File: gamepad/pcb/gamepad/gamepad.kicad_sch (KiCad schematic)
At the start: 13 parts, among them U3 RP2040-ZERO

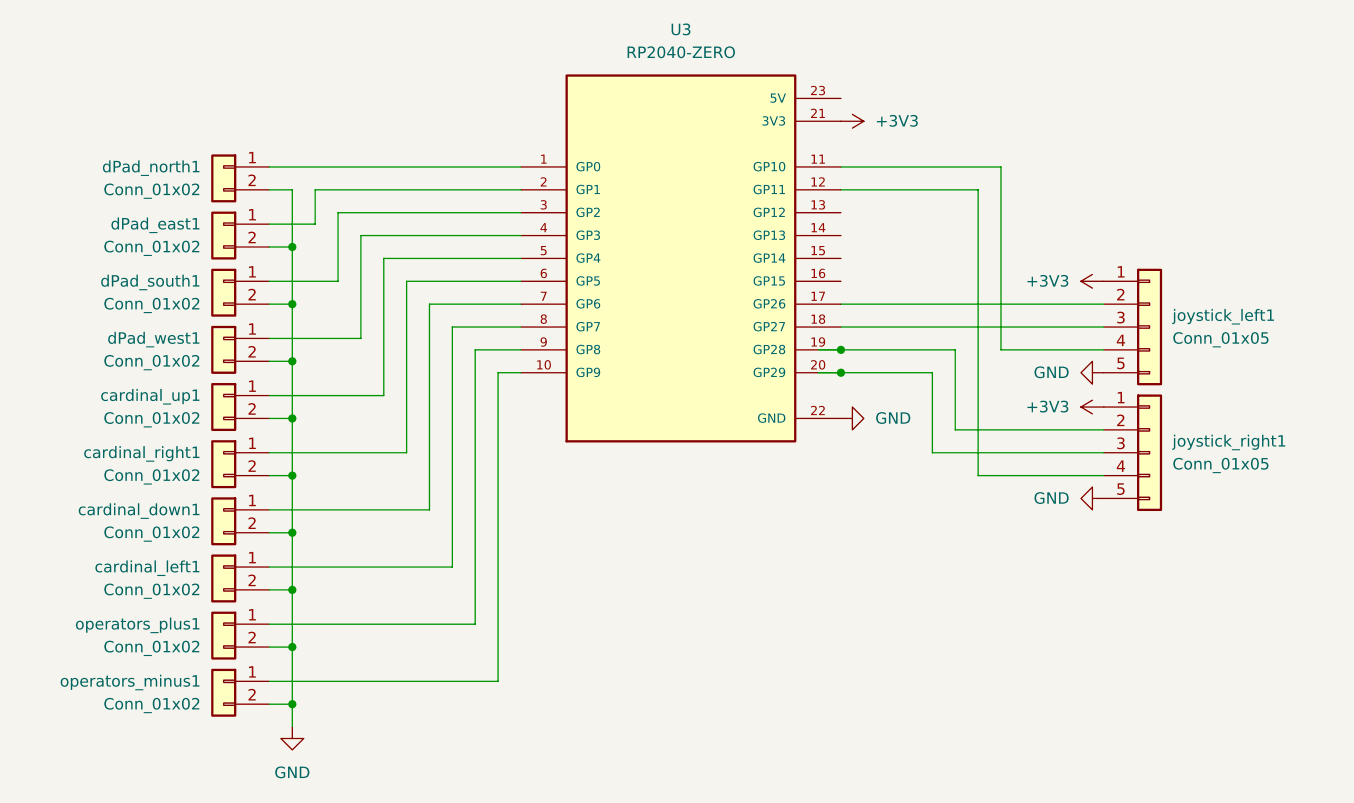
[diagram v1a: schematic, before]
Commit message: feat: smaller pcb
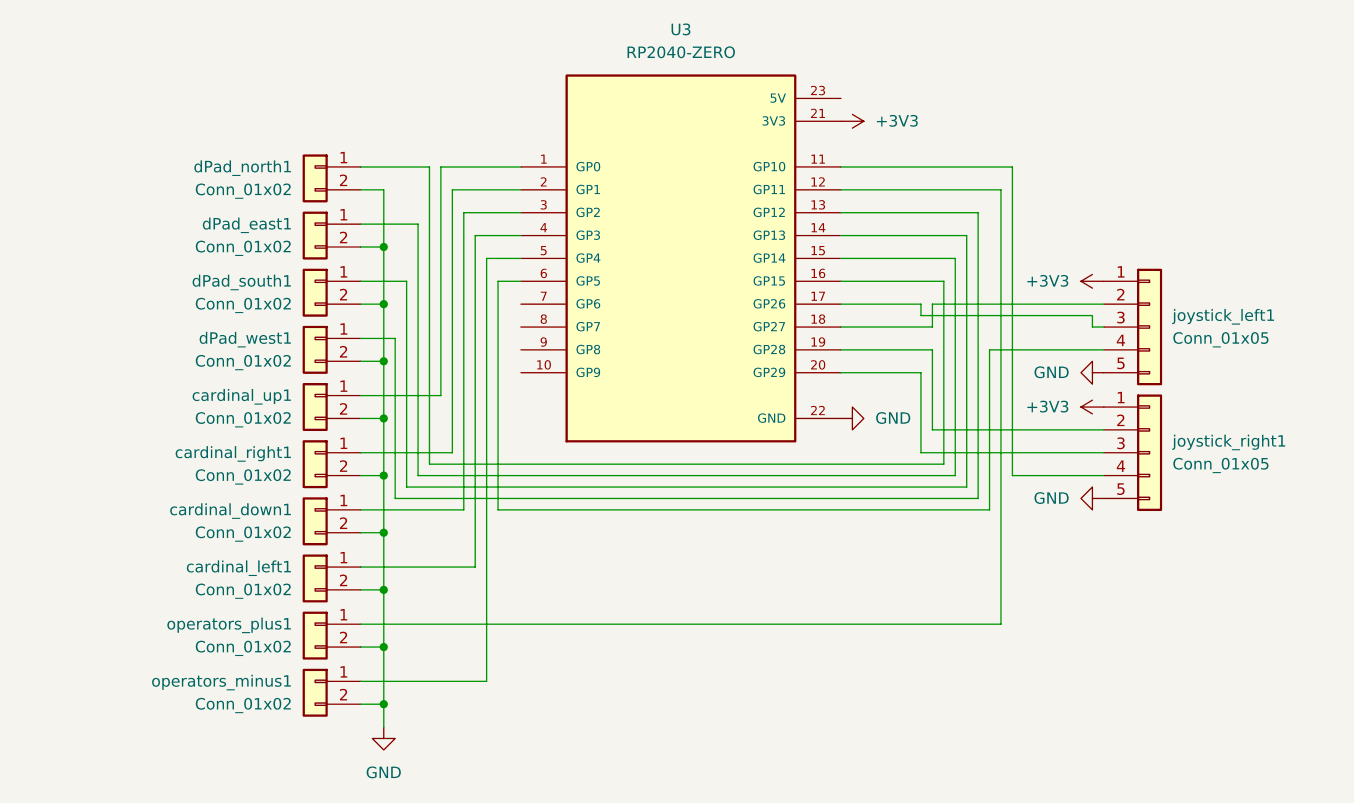
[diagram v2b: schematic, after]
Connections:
- net at operators_plus1.1 (Pin_1): now also U3.12 (GP11); no longer U3.9 (GP8)
- net at U3.1 (GP0): now also cardinal_up1.1 (Pin_1); no longer dPad_north1.1 (Pin_1)
- net at U3.10 (GP9): no longer operators_minus1.1 (Pin_1)
- net at U3.11 (GP10): now also joystick_right1.4 (Pin_4); no longer joystick_left1.4 (Pin_4)
- net at U3.13 (GP12): now also dPad_west1.1 (Pin_1)
- net at U3.14 (GP13): now also dPad_south1.1 (Pin_1)
- net at U3.15 (GP14): now also dPad_east1.1 (Pin_1)
- net at U3.16 (GP15): now also dPad_north1.1 (Pin_1)
- net at U3.17 (GP26): now also joystick_left1.3 (Pin_3); no longer joystick_left1.2 (Pin_2)
- net at U3.18 (GP27): now also joystick_left1.2 (Pin_2); no longer joystick_left1.3 (Pin_3)
- net at U3.2 (GP1): now also cardinal_right1.1 (Pin_1); no longer dPad_east1.1 (Pin_1)
- net at U3.3 (GP2): now also cardinal_down1.1 (Pin_1); no longer dPad_south1.1 (Pin_1)
- net at U3.4 (GP3): now also cardinal_left1.1 (Pin_1); no longer dPad_west1.1 (Pin_1)
- net at U3.5 (GP4): now also operators_minus1.1 (Pin_1); no longer cardinal_up1.1 (Pin_1)
- net at U3.6 (GP5): now also joystick_left1.4 (Pin_4); no longer cardinal_right1.1 (Pin_1)
- net at U3.7 (GP6): no longer cardinal_down1.1 (Pin_1)
- net at U3.8 (GP7): no longer cardinal_left1.1 (Pin_1)
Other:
- moved on the sheet: cardinal_down1, cardinal_left1, cardinal_right1, cardinal_up1, dPad_east1, dPad_north1, dPad_south1, dPad_west1, operators_minus1, operators_plus1

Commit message: fix: swap pcb left/right
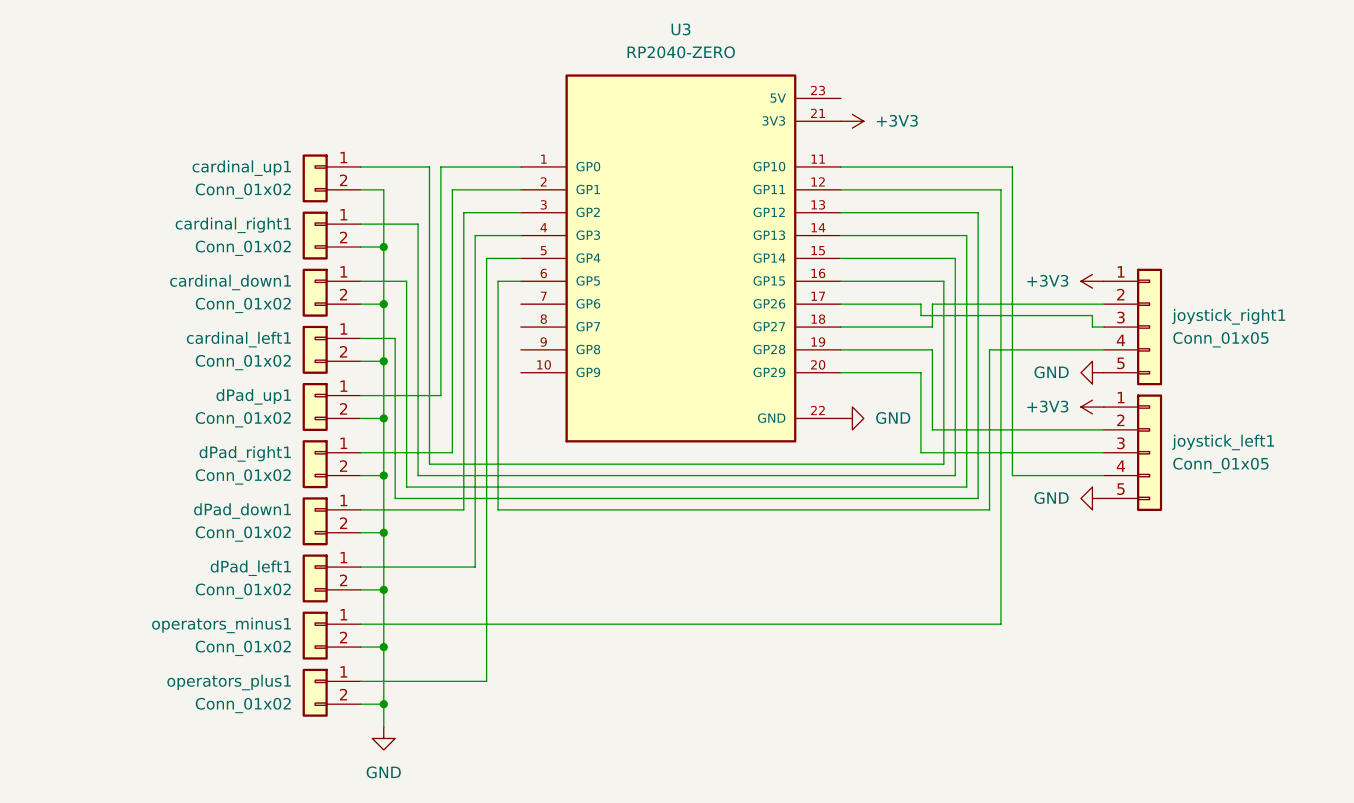
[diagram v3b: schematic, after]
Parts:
- renumbered dPad_south1 to cardinal_down1, dPad_west1 to cardinal_left1, dPad_east1 to cardinal_right1, dPad_north1 to cardinal_up1, cardinal_down1 to dPad_down1, cardinal_left1 to dPad_left1, cardinal_right1 to dPad_right1, cardinal_up1 to dPad_up1, joystick_right1 to joystick_left1, joystick_left1 to joystick_right1, operators_plus1 to operators_minus1, operators_minus1 to operators_plus1
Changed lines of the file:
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@@
 		(dnp no)
 		(fields_autoplaced yes)
-		(property "Reference" "operators_plus1"
+		(property "Reference" "operators_minus1"
 			(at 58.42 96.5199 0)
 			(effects
@@
 			(project "gamepad"
 				(path "/00bcd25f-2f85-4197-8989-5ad786ea0927"
-					(reference "operators_plus1")
+					(reference "operators_minus1")
 					(unit 1)
 				)
@@
 		(dnp no)
 		(fields_autoplaced yes)
-		(property "Reference" "dPad_east1"
+		(property "Reference" "cardinal_right1"
 			(at 58.42 52.0699 0)
 			(effects
@@
 			(project "gamepad"
 				(path "/00bcd25f-2f85-4197-8989-5ad786ea0927"
-					(reference "dPad_east1")
+					(reference "cardinal_right1")
 					(unit 1)
 				)
@@
 		(dnp no)
 		(fields_autoplaced yes)
-		(property "Reference" "joystick_left1"
+		(property "Reference" "joystick_right1"
 			(at 156.21 62.2299 0)
 			(effects
@@
 			(project ""
 				(path "/00bcd25f-2f85-4197-8989-5ad786ea0927"
-					(reference "joystick_left1")
+					(reference "joystick_right1")
 					(unit 1)
 				)
@@
 		(dnp no)
 		(fields_autoplaced yes)
-		(property "Reference" "cardinal_down1"
+		(property "Reference" "dPad_down1"
 			(at 58.42 83.8199 0)
 			(effects
@@
 			(project "gamepad"
 				(path "/00bcd25f-2f85-4197-8989-5ad786ea0927"
-					(reference "cardinal_down1")
+					(reference "dPad_down1")
 					(unit 1)
 				)
@@
 		(dnp no)
 		(fields_autoplaced yes)
-		(property "Reference" "dPad_south1"
+		(property "Reference" "cardinal_down1"
 			(at 58.42 58.4199 0)
 			(effects
@@
 			(project "gamepad"
 				(path "/00bcd25f-2f85-4197-8989-5ad786ea0927"
-					(reference "dPad_south1")
+					(reference "cardinal_down1")
 					(unit 1)
 				)
@@
 		(dnp no)
 		(fields_autoplaced yes)
-		(property "Reference" "dPad_north1"
+		(property "Reference" "cardinal_up1"
 			(at 58.42 45.7199 0)
 			(effects
@@
 			(project ""
 				(path "/00bcd25f-2f85-4197-8989-5ad786ea0927"
-					(reference "dPad_north1")
+					(reference "cardinal_up1")
 					(unit 1)
 				)
@@
 		(dnp no)
 		(fields_autoplaced yes)
-		(property "Reference" "joystick_right1"
+		(property "Reference" "joystick_left1"
 			(at 156.21 76.1999 0)
 			(effects
@@
 			(project "gamepad"
 				(path "/00bcd25f-2f85-4197-8989-5ad786ea0927"
-					(reference "joystick_right1")
+					(reference "joystick_left1")
 					(unit 1)
 				)
@@
 		(dnp no)
 		(fields_autoplaced yes)
-		(property "Reference" "operators_minus1"
+		(property "Reference" "operators_plus1"
 			(at 58.42 102.8699 0)
 			(effects
@@
 			(project "gamepad"
 				(path "/00bcd25f-2f85-4197-8989-5ad786ea0927"
-					(reference "operators_minus1")
+					(reference "operators_plus1")
 					(unit 1)
 				)
@@
 		(dnp no)
 		(fields_autoplaced yes)
-		(property "Reference" "cardinal_left1"
+		(property "Reference" "dPad_left1"
 			(at 58.42 90.1699 0)
 			(effects
@@
 			(project "gamepad"
 				(path "/00bcd25f-2f85-4197-8989-5ad786ea0927"
-					(reference "cardinal_left1")
+					(reference "dPad_left1")
 					(unit 1)
 				)
@@
 		(dnp no)
 		(fields_autoplaced yes)
-		(property "Reference" "cardinal_up1"
+		(property "Reference" "dPad_up1"
 			(at 58.42 71.1199 0)
 			(effects
@@
 			(project "gamepad"
 				(path "/00bcd25f-2f85-4197-8989-5ad786ea0927"
-					(reference "cardinal_up1")
+					(reference "dPad_up1")
 					(unit 1)
 				)
@@
 		(dnp no)
 		(fields_autoplaced yes)
-		(property "Reference" "cardinal_right1"
+		(property "Reference" "dPad_right1"
 			(at 58.42 77.4699 0)
 			(effects
@@
 			(project "gamepad"
 				(path "/00bcd25f-2f85-4197-8989-5ad786ea0927"
-					(reference "cardinal_right1")
+					(reference "dPad_right1")
 					(unit 1)
 				)
@@
 		(dnp no)
 		(fields_autoplaced yes)
-		(property "Reference" "dPad_west1"
+		(property "Reference" "cardinal_left1"
 			(at 58.42 64.7699 0)
 			(effects
@@
 			(project "gamepad"
 				(path "/00bcd25f-2f85-4197-8989-5ad786ea0927"
-					(reference "dPad_west1")
-					(unit 1)
-				)
+					(reference "cardinal_left1")
+					(unit 1)
+				)
